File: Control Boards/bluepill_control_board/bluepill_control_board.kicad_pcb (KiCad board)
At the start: 2 copper layers, 65.8 x 34.9 mm, 5 parts, among them J1 Conn_01x26, U1 BluePill_STM32F103C

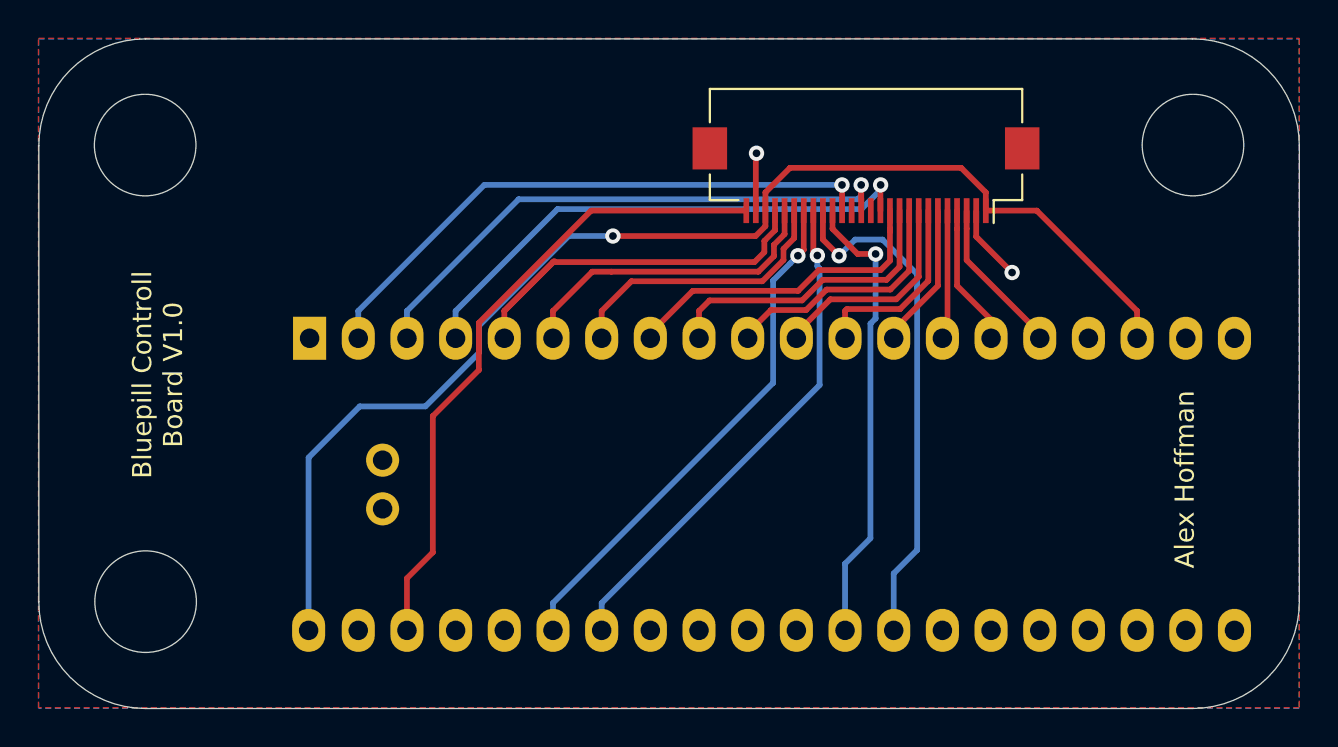
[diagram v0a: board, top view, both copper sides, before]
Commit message: Updated bluepill board for 30pin ribbon cable
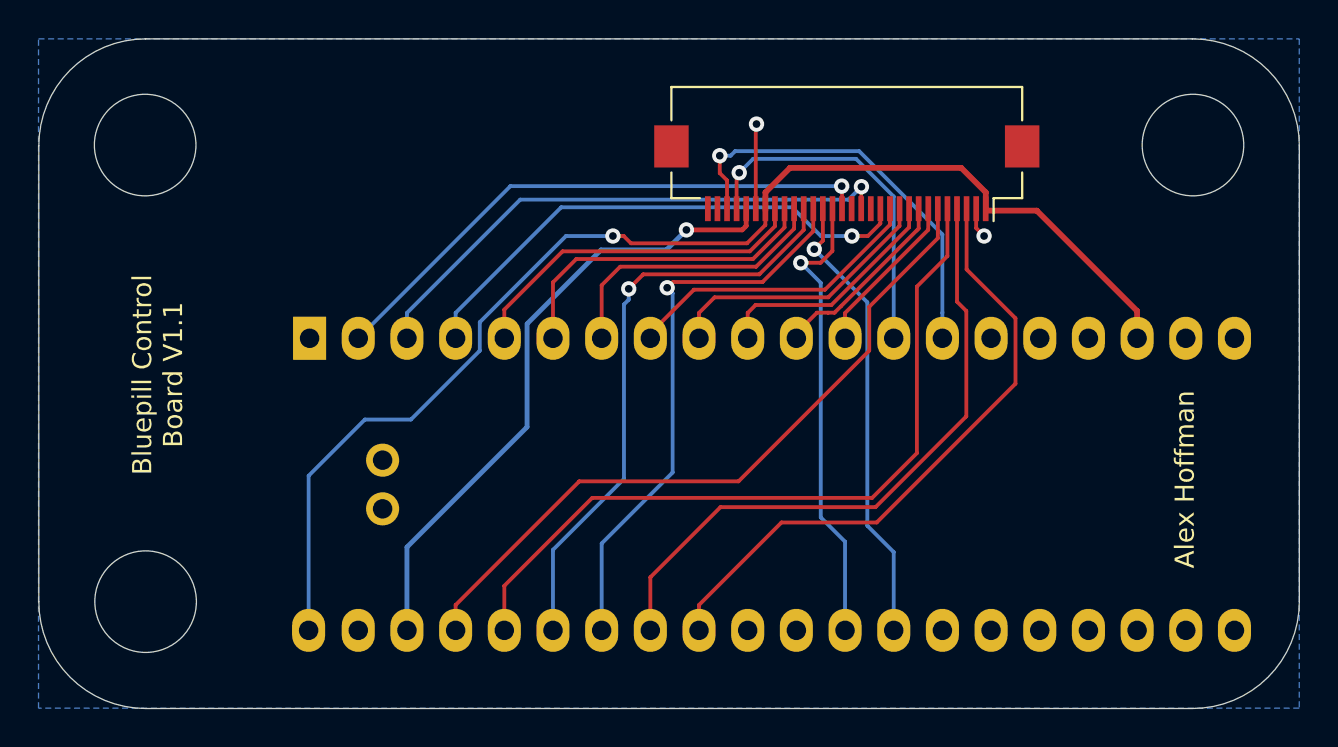
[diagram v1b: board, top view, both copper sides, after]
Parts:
- added G***: LOGO, keyboard:pill, B.Cu at (213.5, 127.4)
- J1: value Conn_01x26 -> Conn_01x30; footprint Connector_FFC-FPC:Hirose_FH12-26S-0.5SH_1x26-1MP_P0.50mm_Horizontal -> Connector_FFC-FPC:Hirose_FH12-30S-0.5SH_1x30-1MP_P0.50mm_Horizontal
- moved J1 1.01 mm to (220.6, 117.1)
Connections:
- U1 pad 13: /MUX3 -> /MOUSE_X
- U1 pad 14: /MUX2 -> /MOUSE_Y
- U1 pad 15: /MUX0 -> Net-(U1-Pad15)
- U1 pad 16: /MUX1 -> Net-(U1-Pad16)
- U1 pad 32: Net-(U1-Pad32) -> /MUX1
- U1 pad 33: Net-(U1-Pad33) -> /MUX0
- U1 pad 36: Net-(U1-Pad36) -> /MUX2
- U1 pad 37: Net-(U1-Pad37) -> /MUX3
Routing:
- net /MUX2: track 6.77 -> 40.1 mm
- net /MUX3: track 7.62 -> 37.3 mm
- net /MUX0: track 7.40 -> 33.8 mm
- net /MUX1: track 8.24 -> 32.8 mm
- net /MOUSE_Y: track 0.00 -> 21.9 mm, vias 0 -> 1
- net /MOUSE_X: track 0.00 -> 18.5 mm, vias 0 -> 1
- net /LED0: track 22.3 -> 18.3 mm
- net /SDA: track 27.3 -> 31.0 mm
- net /USB_D-: track 27.0 -> 23.9 mm
- net /SCL: track 26.7 -> 29.6 mm
- net /ROW4: track 10.1 -> 8.56 mm
- net /ROW3: track 11.3 -> 9.94 mm
- net /ROW1: track 15.8 -> 14.6 mm
- net /RGB4: track 30.7 -> 29.7 mm
- net /ROW0: track 16.9 -> 15.9 mm
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- removed copper zone on F.Cu, net GND
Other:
- board text added: "Bluepill Control Board V1.1"
- board text removed: "Bluepill Controll Board V1.0"

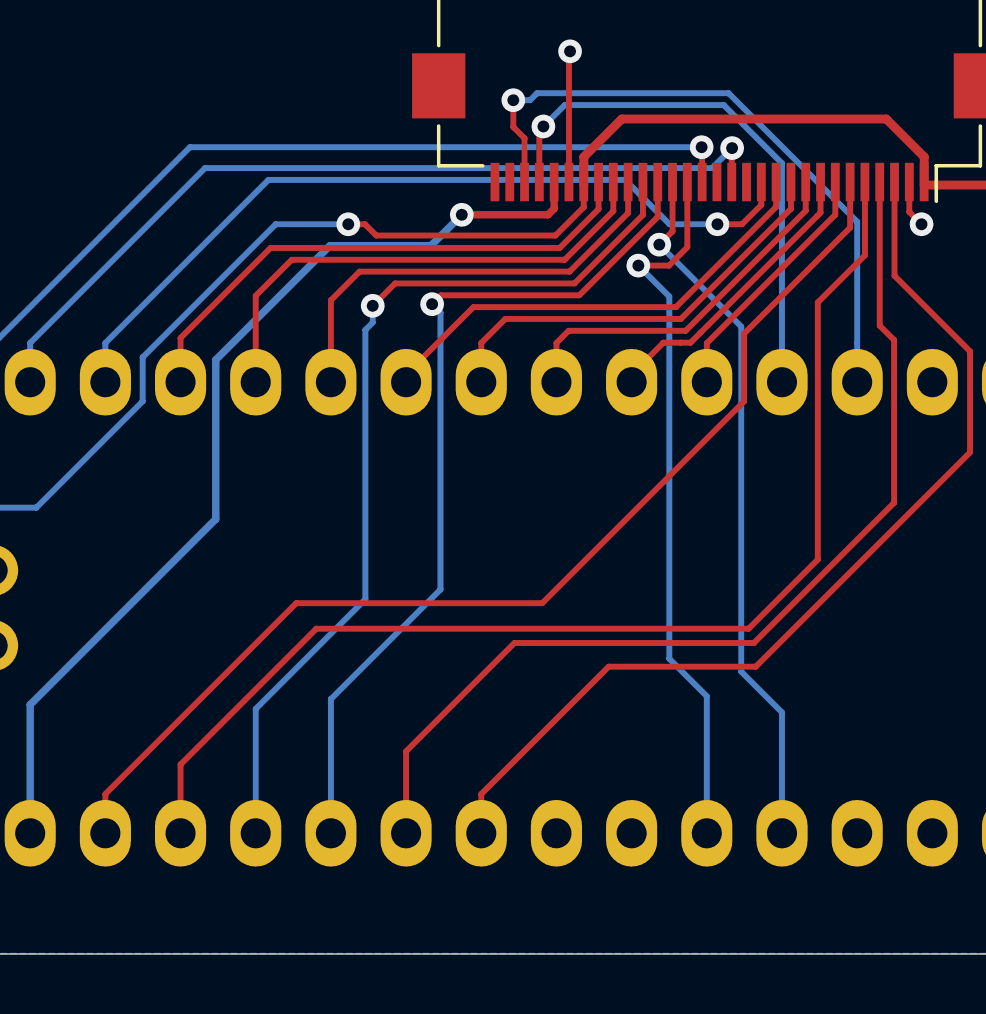
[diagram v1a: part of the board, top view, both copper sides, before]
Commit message: Added BOOT switch
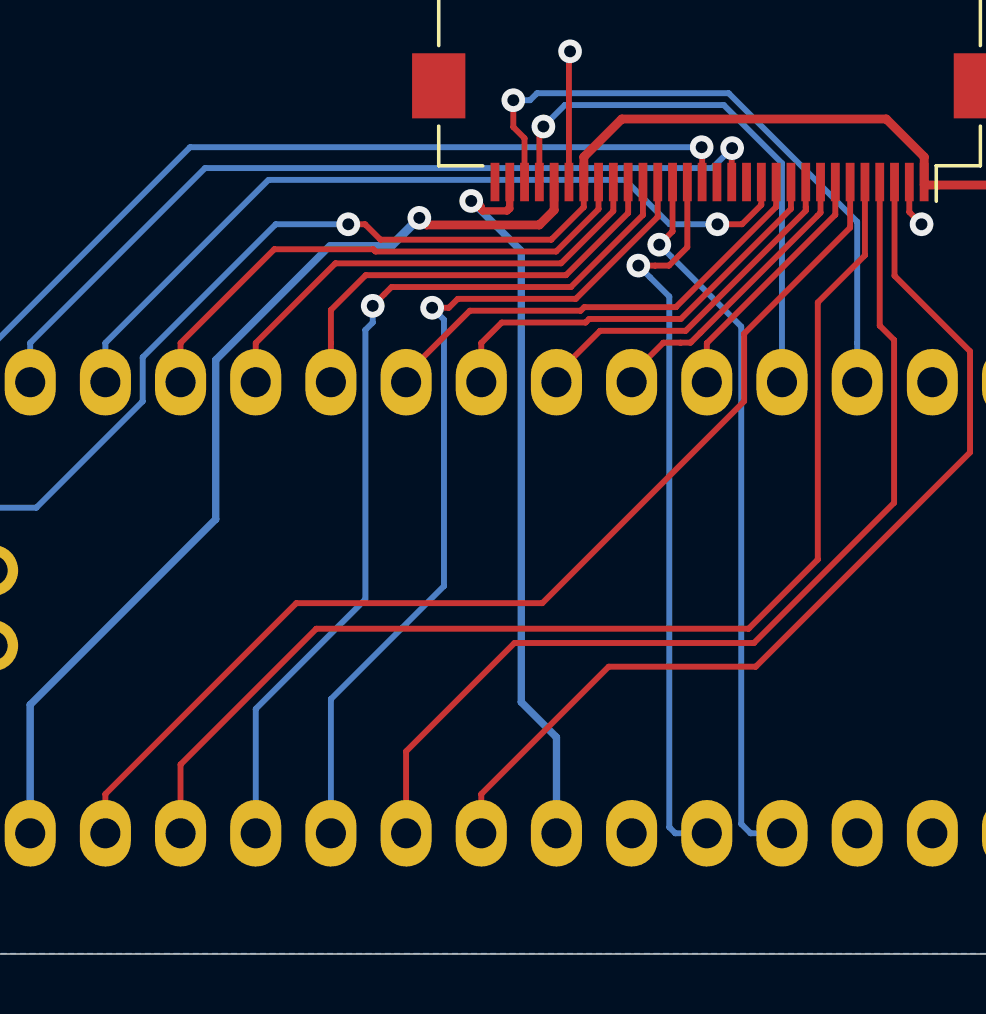
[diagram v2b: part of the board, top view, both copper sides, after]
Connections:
- J1 pad 29: Net-(J1-Pad29) -> /BOOT_SWITCH
- U1 pad 31: Net-(U1-Pad31) -> /BOOT_SWITCH
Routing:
- net /BOOT_SWITCH: track 0.00 -> 25.0 mm, vias 0 -> 1
- net /LED1: track 17.2 -> 16.2 mm
- net /ROW2: track 12.6 -> 11.9 mm
- net /USB_D-: track 23.9 -> 24.5 mm
- net /USB_D+: track 24.3 -> 24.9 mm
